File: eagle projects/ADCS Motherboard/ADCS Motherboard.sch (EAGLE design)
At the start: 120 parts, among them J1 HDR_10_EZFET_DEBUGGER, J3 HDR_2X5_GRPB052VWQS-RC, Q1 PMV16XN, Q2 IRLML6246TRPBF, Q3 IRLML2246TRPBF, U1 MSP430F5529IPN, U2 LMV321, U3 ADS7841E_2K5, U4 LMV321, U5 LMV321, U7 HMC1053, Y1 32.768kHz, Y2 CSTCR4M00G15L99, Y3 32.768kHz

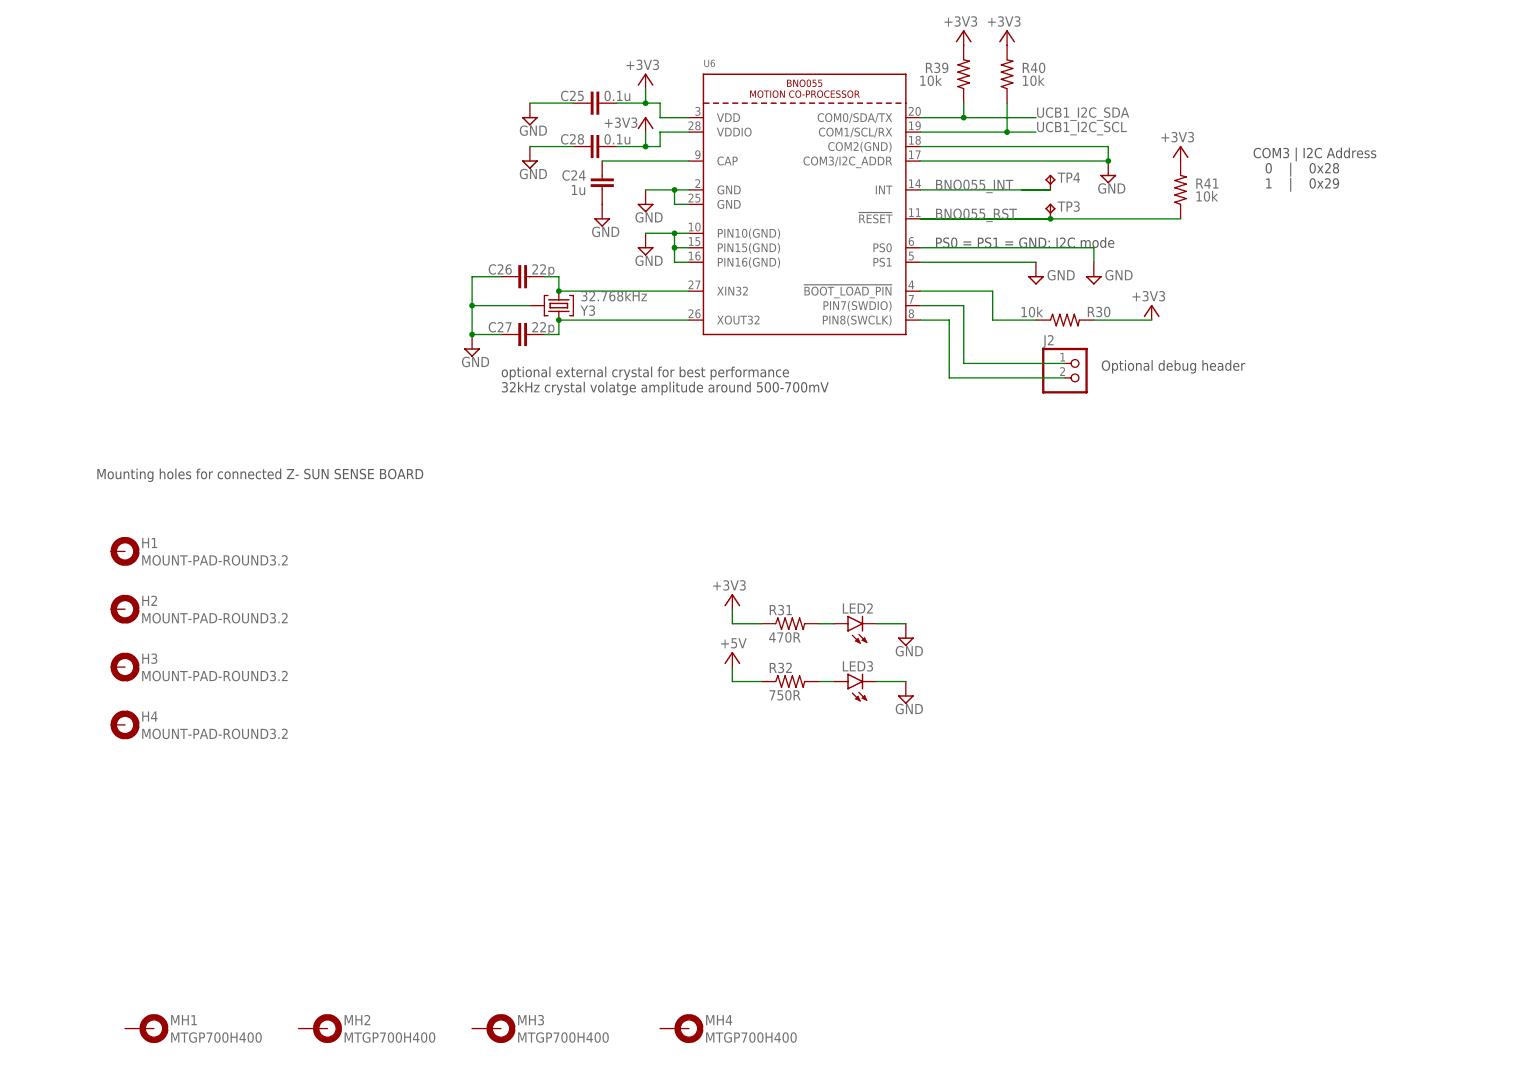
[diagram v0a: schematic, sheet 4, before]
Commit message: Added 5.1M ohms to BNO055 no connect pins
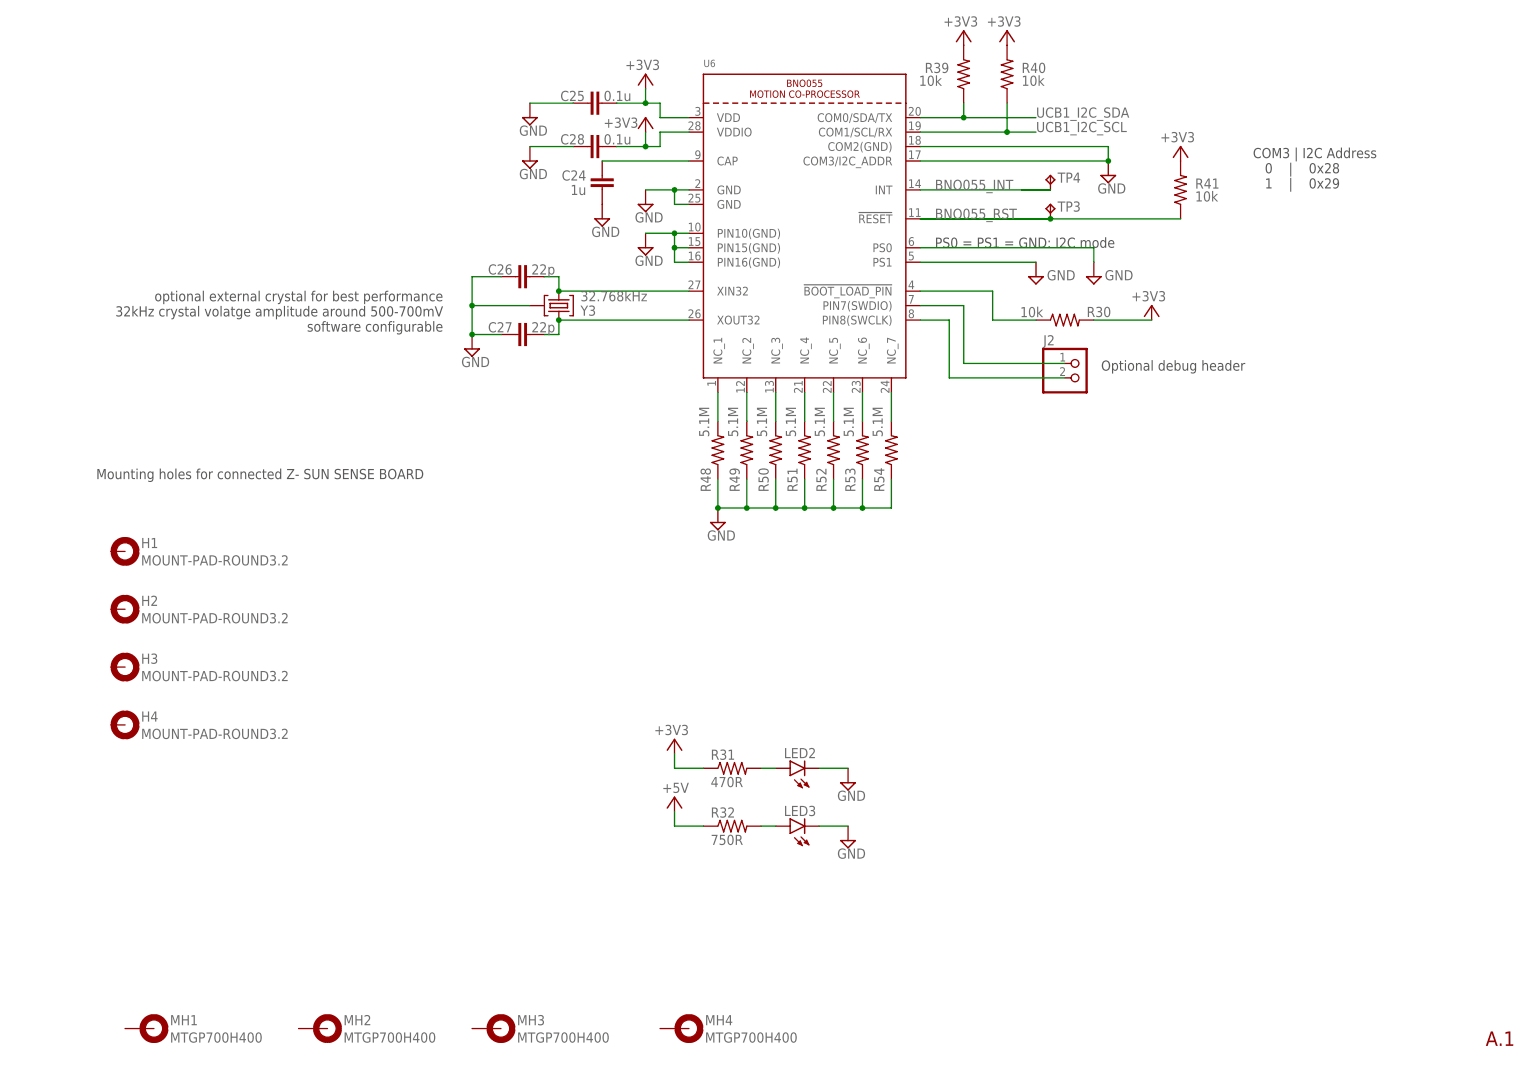
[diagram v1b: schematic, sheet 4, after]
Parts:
- added R48, R49, R50, R51, R52, R53, R54: 5.1M, rcl:R-US_R0402
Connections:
- new net N$40: R48.2, U6.NC_1
- new net N$42: R49.2, U6.NC_2
- new net N$43: R50.2, U6.NC_3
- new net N$44: R51.2, U6.NC_4
- new net N$45: R52.2, U6.NC_5
- new net N$46: R53.2, U6.NC_6
- new net N$47: R54.2, U6.NC_7
- net GND: now also R48.1, R49.1, R50.1, R51.1, R52.1, R53.1, R54.1
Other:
- note added: "A.1"
- note added: "optional external crystal for best performance 32kHz crystal volatge amplitude around 500-700mV software configurable"
- note removed: "optional external crystal for best performance 32kHz crystal volatge amplitude around 500-700mV"
- moved on the sheet: LED2, LED3, R31, R32

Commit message: Major layout changes check point
New connectors, analog plane reshape, moved msp430
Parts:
- removed A3: ARDUCAM_OV5642, my_library:ARDUCAM_OV5642
- removed JP1: (no value), pinhead:PINHD-1X3
- removed JP3: (no value), pinhead:PINHD-2X3
- removed JP6: (no value), my_library:JP1Q_
- removed R44: 5.1M, rcl:R-US_R0402
- added A1: ARDUCAM_OV5642, my_library:ARDUCAM_OV5642
- added J5, J8: CNC_3221-10-0300-00, my_library:CNC_3221-10-0300-00
- added J7: TE-1734829-3, my_library:TE-1734829-3
- added J9: CNC_3221-14-0300-00, my_library:CNC_3221-14-0300-00
- added R55, R56: 5.1M, rcl:R-US_R0603
- added TP10, TP11, TP12, TP13, TP14, TP15, TP16, TP17, TP6, TP7, TP8, TP9: TESTPOINT, my_library:TESTPOINT
- C17, C21, C23: device rcl:C-EUC0805 -> rcl:C-EUC0603
- C18: device resistor:C-EUC1206 -> rcl:C-EUC0805
- J11: value (none) -> CNC_3221-10-0300-00; device my_library:PINHD-1X7 -> my_library:CNC_3221-10-0300-00
- J3: value HDR_2X5_GRPB052VWQS-RC -> CNC_3221-10-0300-00; device my_library:HDR_2X5_GRPB052VWQS-RC -> my_library:CNC_3221-10-0300-00
- J6: device my_library:PINHD-2X8 -> my_library:PINHD-1X3
- JP2: device pinhead:PINHD-2X5 -> my_library:PINHD-1X6
- R10, R11, R12, R13, R14, R15, R17, R18, R20, R21, R22, R23, R24, R25, R26, R27, R28, R29: device rcl:R-US_R0805 -> rcl:R-US_R0603
- R16: value 0R -> 1R
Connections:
- removed net !CS!_CAM_A: A2.CS, J11.1
- removed net !CS!_CAM_B: A3.CS, J11.2
- removed net N$18: JP2.8, R45.1
- removed net N$19: JP2.10, R44.1
- removed net PAYLOAD_MISO: A2.MISO, A3.MISO, J11.4
- removed net PAYLOAD_MOSI: A2.MOSI, A3.MOSI, J11.3
- removed net PAYLOAD_SCL: A2.SCL, A3.SCL, J11.7
- removed net PAYLOAD_SCLK: A2.SCLK, A3.SCLK, J11.5
- removed net PAYLOAD_SDA: A2.SDA, A3.SDA, J11.6
- removed net SEN_BRD_5V_PRESENT: J3.9, R2.1, R3.2
- new net CAMERA-1_CS: A1.CS, J5.6
- new net CAMERA-1_SCL: A1.SCL, J5.2
- new net CAMERA-1_SDA: A1.SDA, J5.4
- new net CAMERA-2_CS: A2.CS, J5.7
- new net CAMERA-2_SCL: A2.SCL, J5.3
- new net CAMERA-2_SDA: A2.SDA, J5.5
- new net CAMERA_MISO: A1.MISO, A2.MISO, J5.8
- new net CAMERA_MOSI: A1.MOSI, A2.MOSI, J5.10
- new net CAMERA_SCLK: A1.SCLK, A2.SCLK, J5.9
- new net CAM_5V_PRESENT: J5.1, R2.1, R3.2
- new net N$55: J8.9, R56.2
- new net N$57: J8.10, R55.1
- new net N$58: J3.8, R45.1
- new net P1.0: JP2.6, U1.P1.0/TA0CLK/ACLK
- new net P1.1: JP2.5, U1.P1.1/TA0.0
- new net TB0.3: JP2.2, U1.P7.5/TB0.3
- new net TB0.4: JP2.1, U1.P7.6/TB0.4
- new net TB0.5: JP2.4, U1.P3.5/TB0.5
- new net TB0.6: JP2.3, U1.P3.6/TB0.6
- new net Z-_SUN_3V_PRESENT: J11.9, J3.10
- net !CS!_CURRENT_SENSE_1: now also J8.3; no longer JP3.1
- net !CS!_CURRENT_SENSE_2: now also J8.5; no longer JP3.3
- net !CS!_SUN_X+: now also J3.2; no longer JP2.2
- net !CS!_SUN_X-: now also J3.7; no longer JP2.7
- net !CS!_SUN_Y+: now also J3.4; no longer JP2.4
- net !CS!_SUN_Y-: now also J3.9; no longer JP2.9
- net !CS!_SUN_Z+: now also JP4.4; no longer JP4.5
- net !CS!_SUN_Z-: now also J3.6; no longer JP2.6
- net +3V3: now also J11.7, J6.2, J7.3V3; no longer J3.7, JP1.2
- net +5V: now also A1.+5V, J6.1, J7.5V; no longer A3.+5V, JP1.1
- net ACT_BRD_3V_PRESENT: now also J11.4, J8.7; no longer J3.4, JP3.5
- net ACT_BRD_5V_PRESENT: now also J9.14; no longer J6.14
- net ACT_BRD_5V_SHIFTED: now also J11.2; no longer J3.2
- net B_MEAS_X: now also TP10.TP
- net B_MEAS_Y: now also TP9.TP
- net B_MEAS_Z: now also TP11.TP
- net GND: now also A1.GND, A1.MTG_1, A1.MTG_2, A2.MTG_1, A2.MTG_2, J6.3, J7.GND, R55.2, R56.1; no longer A3.GND, JP1.3, R44.2
- net MAG_X_FIN: now also J9.10; no longer J6.10
- net MAG_X_RIN: now also J9.12; no longer J6.12
- net MAG_Y_FIN: now also J9.6; no longer J6.6
- net MAG_Y_RIN: now also J9.8; no longer J6.8
- net MAG_Z_FIN: now also J9.2; no longer J6.2
- net MAG_Z_RIN: now also J9.4; no longer J6.4
- net MSP430_ACTIVE: now also J11.10; no longer J3.10
- net MSP_OBC_RESET: now also J11.5; no longer J3.5
- net N$35: now also TP8.TP; no longer JP6.2
- net N$37: now also TP7.TP; no longer JP6.1
- net N$9: now also TP6.TP
- net OUT_A_N: now also TP13.TP
- net OUT_A_P: now also TP12.TP
- net OUT_B_N: now also TP15.TP
- net OUT_B_P: now also TP14.TP
- net OUT_C_N: now also TP17.TP
- net OUT_C_P: now also TP16.TP
- net RESERVED_1: now also J11.6; no longer J3.6
- net RESERVED_2: now also J11.8; no longer J3.8
- net RW_X_DIR: now also J9.7; no longer J6.7
- net RW_X_OUTFG: now also J9.13; no longer J6.13
- net RW_X_SPEED_CTRL: now also J9.1; no longer J6.1
- net RW_Y_DIR: now also J9.9; no longer J6.9
- net RW_Y_OUTFG: now also J8.1; no longer J6.15
- net RW_Y_SPEED_CTRL: now also J9.3; no longer J6.3
- net RW_Z_DIR: now also J9.11; no longer J6.11
- net RW_Z_OUTFG: now also J8.2; no longer J6.16
- net RW_Z_SPEED_CTRL: now also J9.5; no longer J6.5
- net UCA0RXD: now also J11.1; no longer J3.1
- net UCA0TXD: now also J11.3; no longer J3.3
- net UCB0_SPI_CLK: now also J3.5, J8.4, JP4.5; no longer JP2.5, JP3.2, JP4.4
- net UCB0_SPI_MISO: now also J3.1, J8.6; no longer JP2.1, JP3.4
- net UCB0_SPI_MOSI: now also J3.3, J8.8; no longer JP2.3, JP3.6
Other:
- note added: "PWM_IN"
- note added: "PWM_OUT"
- note added: "Z+ SUN SENSE BOARD CONNECTOR"
- note added: "Z- SUN SENSE BOARD CONNECTOR"
- moved on the sheet: J3, J4, LED1, R16, R2, R3, R4, R45, R5, R8

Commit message: Draft of Rev B done
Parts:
- added TP18, TP19: TESTPOINT, my_library:TESTPOINT
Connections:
- net P1.0: now also JP2.1; no longer JP2.6
- net P1.1: now also JP2.2; no longer JP2.5
- net TB0.3: now also JP2.5; no longer JP2.2
- net TB0.4: now also JP2.6; no longer JP2.1
- net TB0.5: now also JP2.3; no longer JP2.4
- net TB0.6: now also JP2.4; no longer JP2.3
- net UCB1_I2C_SCL: now also TP18.TP
- net UCB1_I2C_SDA: now also TP19.TP
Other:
- moved on the sheet: JP2
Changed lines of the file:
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@@
 <setting verticaltext="up"/>
 </settings>
-<grid distance="0.1" unitdist="inch" unit="inch" style="lines" multiple="1" display="no" altdistance="0.05" altunitdist="inch" altunit="inch"/>
+<grid distance="0.1" unitdist="inch" unit="inch" style="lines" multiple="1" display="no" altdistance="0.01" altunitdist="inch" altunit="inch"/>
 <layers>
 <layer number="1" name="Top" color="4" fill="1" visible="no" active="no"/>
@@
 <part name="P+6" library="supply1" library_urn="urn:adsk.eagle:library:371" deviceset="+5V" device=""/>
 <part name="P+7" library="supply1" library_urn="urn:adsk.eagle:library:371" deviceset="+5V" device=""/>
-<part name="J3" library="my_library" library_urn="urn:adsk.eagle:library:22876504" deviceset="CNC_3221-10-0300-00" device=""/>
-<part name="J9" library="my_library" library_urn="urn:adsk.eagle:library:22876504" deviceset="CNC_3221-14-0300-00" device=""/>
-<part name="J8" library="my_library" library_urn="urn:adsk.eagle:library:22876504" deviceset="CNC_3221-10-0300-00" device=""/>
-<part name="J11" library="my_library" library_urn="urn:adsk.eagle:library:22876504" deviceset="CNC_3221-10-0300-00" device=""/>
+<part name="J3" library="my_library" library_urn="urn:adsk.eagle:library:22876504" deviceset="CNC_3221-10-0300-00" device="" package3d_urn="urn:adsk.eagle:package:27602901/2"/>
+<part name="J9" library="my_library" library_urn="urn:adsk.eagle:library:22876504" deviceset="CNC_3221-14-0300-00" device="" package3d_urn="urn:adsk.eagle:package:27621415/1"/>
+<part name="J8" library="my_library" library_urn="urn:adsk.eagle:library:22876504" deviceset="CNC_3221-10-0300-00" device="" package3d_urn="urn:adsk.eagle:package:27602901/2"/>
+<part name="J11" library="my_library" library_urn="urn:adsk.eagle:library:22876504" deviceset="CNC_3221-10-0300-00" device="" package3d_urn="urn:adsk.eagle:package:27602901/2"/>
 <part name="SUPPLY9" library="supply2" library_urn="urn:adsk.eagle:library:372" deviceset="GND" device=""/>
-<part name="J7" library="my_library" library_urn="urn:adsk.eagle:library:22876504" deviceset="TE-1734829-3" device="" package3d_urn="urn:adsk.eagle:package:27602903/1"/>
+<part name="J7" library="my_library" library_urn="urn:adsk.eagle:library:22876504" deviceset="TE-1734829-3" device="" package3d_urn="urn:adsk.eagle:package:27602903/2"/>
 <part name="P+4" library="supply1" library_urn="urn:adsk.eagle:library:371" deviceset="+5V" device=""/>
 <part name="+3V3" library="supply1" library_urn="urn:adsk.eagle:library:371" deviceset="+3V3" device=""/>
 <part name="SUPPLY10" library="supply2" library_urn="urn:adsk.eagle:library:372" deviceset="GND" device=""/>
-<part name="J5" library="my_library" library_urn="urn:adsk.eagle:library:22876504" deviceset="CNC_3221-10-0300-00" device=""/>
+<part name="J5" library="my_library" library_urn="urn:adsk.eagle:library:22876504" deviceset="CNC_3221-10-0300-00" device="" package3d_urn="urn:adsk.eagle:package:27602901/2"/>
 <part name="J6" library="my_library" library_urn="urn:adsk.eagle:library:22876504" deviceset="PINHD-1X3" device="" package3d_urn="urn:adsk.eagle:package:24583855/1"/>
 <part name="R55" library="rcl" library_urn="urn:adsk.eagle:library:334" deviceset="R-US_" device="R0603" package3d_urn="urn:adsk.eagle:package:23555/3" value="5.1M"/>
@@
 <part name="SUPPLY57" library="supply2" library_urn="urn:adsk.eagle:library:372" deviceset="GND" device=""/>
 <part name="JP2" library="my_library" library_urn="urn:adsk.eagle:library:22876504" deviceset="PINHD-1X6" device="" package3d_urn="urn:adsk.eagle:package:26872615/1"/>
+<part name="TP18" library="my_library" library_urn="urn:adsk.eagle:library:22876504" deviceset="TESTPOINT" device="" package3d_urn="urn:adsk.eagle:package:24605432/3"/>
+<part name="TP19" library="my_library" library_urn="urn:adsk.eagle:library:22876504" deviceset="TESTPOINT" device="" package3d_urn="urn:adsk.eagle:package:24605432/3"/>
 </parts>
 <sheets>
@@
 <attribute name="VALUE" x="219.075" y="122.555" size="1.778" layer="96" rot="R90"/>
 </instance>
-<instance part="JP2" gate="A" x="266.7" y="86.36" smashed="yes">
-<attribute name="NAME" x="260.35" y="97.155" size="1.778" layer="95"/>
-<attribute name="VALUE" x="260.35" y="76.2" size="1.778" layer="96"/>
+<instance part="JP2" gate="A" x="269.24" y="86.36" smashed="yes">
+<attribute name="NAME" x="262.89" y="97.155" size="1.778" layer="95"/>
+<attribute name="VALUE" x="262.89" y="76.2" size="1.778" layer="96"/>
+</instance>
+<instance part="TP18" gate="G$1" x="210.82" y="60.96" smashed="yes">
+<attribute name="NAME" x="209.55" y="62.23" size="1.778" layer="95"/>
+</instance>
+<instance part="TP19" gate="G$1" x="208.28" y="55.88" smashed="yes">
+<attribute name="NAME" x="207.01" y="57.15" size="1.778" layer="95"/>
 </instance>
 </instances>
@@
 <wire x1="170.18" y1="73.66" x2="208.28" y2="73.66" width="0.1524" layer="91"/>
 <wire x1="208.28" y1="73.66" x2="208.28" y2="58.42" width="0.1524" layer="91"/>
-<wire x1="208.28" y1="58.42" x2="213.36" y2="58.42" width="0.1524" layer="91"/>
+<wire x1="208.28" y1="58.42" x2="210.82" y2="58.42" width="0.1524" layer="91"/>
 <label x="213.36" y="58.42" size="1.778" layer="95" xref="yes"/>
+<pinref part="TP18" gate="G$1" pin="TP"/>
+<wire x1="210.82" y1="58.42" x2="213.36" y2="58.42" width="0.1524" layer="91"/>
+<junction x="210.82" y="58.42"/>
 </segment>
 </net>
@@
 <wire x1="170.18" y1="71.12" x2="205.74" y2="71.12" width="0.1524" layer="91"/>
 <wire x1="205.74" y1="71.12" x2="205.74" y2="53.34" width="0.1524" layer="91"/>
-<wire x1="205.74" y1="53.34" x2="213.36" y2="53.34" width="0.1524" layer="91"/>
+<wire x1="205.74" y1="53.34" x2="208.28" y2="53.34" width="0.1524" layer="91"/>
 <label x="213.36" y="53.34" size="1.778" layer="95" xref="yes"/>
+<pinref part="TP19" gate="G$1" pin="TP"/>
+<wire x1="208.28" y1="53.34" x2="213.36" y2="53.34" width="0.1524" layer="91"/>
+<junction x="208.28" y="53.34"/>
 </segment>
 </net>
@@
 <pinref part="U1" gate="G$1" pin="P7.5/TB0.3"/>
 <wire x1="170.18" y1="101.6" x2="226.06" y2="101.6" width="0.1524" layer="91"/>
-<wire x1="226.06" y1="101.6" x2="226.06" y2="91.44" width="0.1524" layer="91"/>
-<wire x1="226.06" y1="91.44" x2="264.16" y2="91.44" width="0.1524" layer="91"/>
-<pinref part="JP2" gate="A" pin="2"/>
-<label x="248.92" y="91.44" size="1.778" layer="95"/>
+<label x="175.26" y="101.6" size="1.778" layer="95"/>
+</segment>
+<segment>
+<wire x1="251.46" y1="83.82" x2="266.7" y2="83.82" width="0.1524" layer="91"/>
+<label x="251.46" y="83.82" size="1.778" layer="95"/>
+<pinref part="JP2" gate="A" pin="5"/>
 </segment>
 </net>
@@
 <pinref part="U1" gate="G$1" pin="P7.6/TB0.4"/>
 <wire x1="170.18" y1="104.14" x2="228.6" y2="104.14" width="0.1524" layer="91"/>
-<wire x1="228.6" y1="104.14" x2="228.6" y2="93.98" width="0.1524" layer="91"/>
-<wire x1="228.6" y1="93.98" x2="264.16" y2="93.98" width="0.1524" layer="91"/>
-<pinref part="JP2" gate="A" pin="1"/>
-<label x="248.92" y="93.98" size="1.778" layer="95"/>
+<label x="175.26" y="104.14" size="1.778" layer="95"/>
+</segment>
+<segment>
+<wire x1="251.46" y1="81.28" x2="266.7" y2="81.28" width="0.1524" layer="91"/>
+<label x="251.46" y="81.28" size="1.778" layer="95"/>
+<pinref part="JP2" gate="A" pin="6"/>
 </segment>
 </net>
@@
 <wire x1="198.12" y1="63.5" x2="198.12" y2="48.26" width="0.1524" layer="91"/>
 <wire x1="198.12" y1="48.26" x2="238.76" y2="48.26" width="0.1524" layer="91"/>
-<wire x1="238.76" y1="48.26" x2="238.76" y2="88.9" width="0.1524" layer="91"/>
-<wire x1="238.76" y1="88.9" x2="264.16" y2="88.9" width="0.1524" layer="91"/>
-<pinref part="JP2" gate="A" pin="3"/>
-<label x="248.92" y="88.9" size="1.778" layer="95"/>
+<label x="175.26" y="63.5" size="1.778" layer="95"/>
+</segment>
+<segment>
+<pinref part="JP2" gate="A" pin="4"/>
+<wire x1="241.3" y1="86.36" x2="266.7" y2="86.36" width="0.1524" layer="91"/>
+<label x="248.92" y="86.36" size="1.778" layer="95"/>
 </segment>
 </net>
@@
 <wire x1="195.58" y1="60.96" x2="195.58" y2="45.72" width="0.1524" layer="91"/>
 <wire x1="195.58" y1="45.72" x2="241.3" y2="45.72" width="0.1524" layer="91"/>
-<wire x1="241.3" y1="45.72" x2="241.3" y2="86.36" width="0.1524" layer="91"/>
-<wire x1="241.3" y1="86.36" x2="264.16" y2="86.36" width="0.1524" layer="91"/>
-<pinref part="JP2" gate="A" pin="4"/>
-<label x="248.92" y="86.36" size="1.778" layer="95"/>
+<label x="175.26" y="60.96" size="1.778" layer="95"/>
+</segment>
+<segment>
+<pinref part="JP2" gate="A" pin="3"/>
+<wire x1="238.76" y1="88.9" x2="266.7" y2="88.9" width="0.1524" layer="91"/>
+<label x="248.92" y="88.9" size="1.778" layer="95"/>
 </segment>
 </net>
@@
 </segment>
 <segment>
-<wire x1="251.46" y1="83.82" x2="264.16" y2="83.82" width="0.1524" layer="91"/>
-<label x="251.46" y="83.82" size="1.778" layer="95"/>
-<pinref part="JP2" gate="A" pin="5"/>
+<pinref part="JP2" gate="A" pin="2"/>
+<wire x1="226.06" y1="91.44" x2="266.7" y2="91.44" width="0.1524" layer="91"/>
+<label x="248.92" y="91.44" size="1.778" layer="95"/>
 </segment>
 </net>
@@
 </segment>
 <segment>
-<wire x1="251.46" y1="81.28" x2="264.16" y2="81.28" width="0.1524" layer="91"/>
-<label x="251.46" y="81.28" size="1.778" layer="95"/>
-<pinref part="JP2" gate="A" pin="6"/>
-</segment>
-</net>
+<pinref part="JP2" gate="A" pin="1"/>
+<wire x1="228.6" y1="93.98" x2="266.7" y2="93.98" width="0.1524" layer="91"/>
+<label x="248.92" y="93.98" size="1.778" layer="95"/>
+</segment>
+</net>
